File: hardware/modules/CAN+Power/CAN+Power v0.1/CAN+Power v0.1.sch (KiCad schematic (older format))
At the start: 10 parts

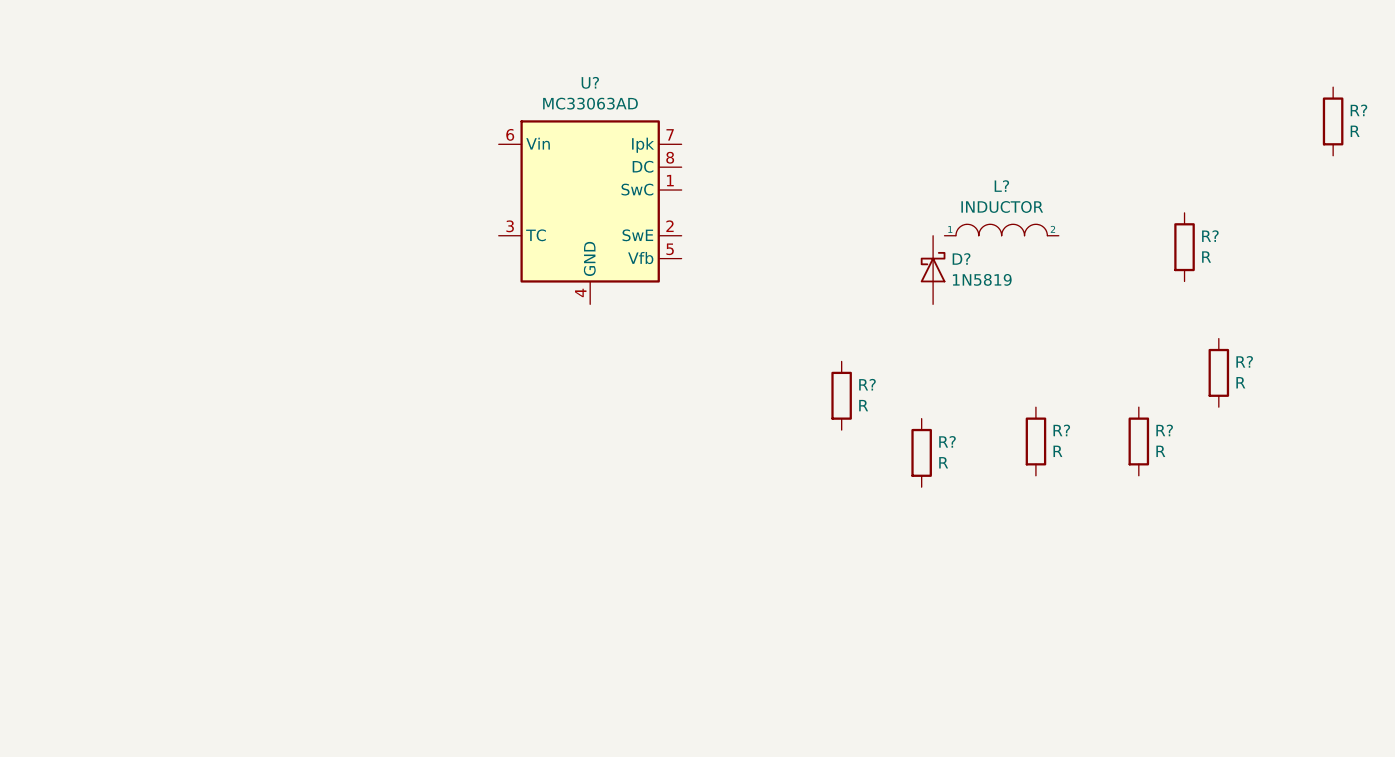
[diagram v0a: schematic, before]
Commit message: добавил керамику на входе, начал схему
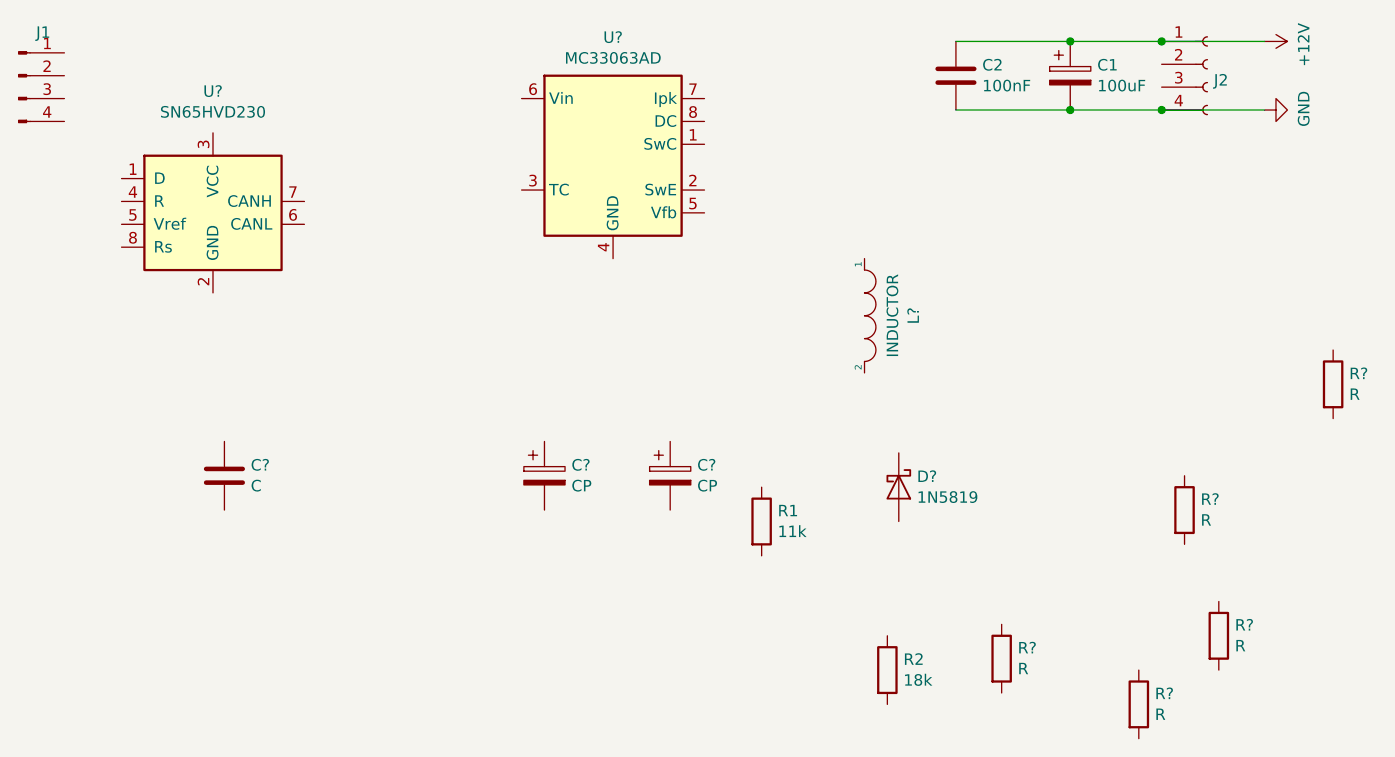
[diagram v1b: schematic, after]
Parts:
- added C1: 100uF, symbol Device:CP
- added C2: 100nF, symbol Device:C
- added C?: C, symbol Device:C
- added C? (x2): CP, symbol Device:CP
- added J1: Conn_01x04_Male, symbol Connector:Conn_01x04_Male
- added J2: 1, symbol Connector:Conn_01x04_Female
- added U?: SN65HVD230, Package_SO:SOIC-8_3.9x4.9mm_P1.27mm, symbol Interface_CAN_LIN:SN65HVD230
- R1: renamed from R?; value R -> 11k
- R2: renamed from R?; value R -> 18k
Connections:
- new net +12V: C1.1, C2.1, J2.1 (Pin_1)
- new net GND: C1.2, C2.2, J2.4 (Pin_4)
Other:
- moved on the sheet: D?, L?, R1, R2, R?, U?

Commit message: готова схема dc\dc
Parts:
- 220uF: renamed from C?; value CP -> C0
- Ct: renamed from C?; value C -> 270pF
- L1: renamed from L?; value INDUCTOR -> 47uH
- Rsc: renamed from R?; value R -> 0.3 Ohm
- gave numbers to parts that had none: 2
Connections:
- net +12V is gone; now on an unnamed net: C1.1, C2.1, J2.1 (Pin_1)
- net GND: now also 220uF.2, Ct.2, D?.2 (A), R1.2, U1.2 (GND), U2.4 (GND); no longer C1.2, C2.2, J2.4 (Pin_4)
- net at U2.1 (SwC): now also Rsc.2, U2.7 (Ipk), U2.8 (DC)
- net at U2.2 (SwE): now also D?.1 (K), L1.1
- net at U2.3 (TC): now also Ct.1
- net at U2.5 (Vfb): now also R1.1, R2.1
- net at U2.6 (Vin): now also Rsc.1
- net at L1.2: now also 220uF.1, R2.2
- new net: C1.2, C2.2, J2.4 (Pin_4)
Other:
- moved on the sheet: 220uF, C1, C2, C?, Ct, D?, J1, L1, R1, R2, R?, Rsc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

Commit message: готова
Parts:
- removed C?: CP, symbol Device:CP
- removed J1: Conn_01x04_Male, symbol Connector:Conn_01x04_Male
- removed R? (x3): R, symbol Device:R
- added C3: 100nF, symbol Device:C
- added C4, C5: 33pF, symbol Device:C
- added FL1: EMI_Filter_LL, symbol Device:EMI_Filter_LL
- added J1: Conn_01x05_Male, symbol Connector:Conn_01x05_Male
- Rterm: renamed from R?; value R -> 120 Ohm
- С0: renamed from 220uF; value C0 -> 220uF
- gave numbers to parts that had none: 1
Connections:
- net CANH: now also Rterm.2, C5.2, FL1.2
- net CANL: now also Rterm.1, C4.2, FL1.4
- net GND: now also C3.1, C4.1, C5.1, J1.1 (Pin_1)
- net 3.3+: now reaches L1.2, R2.2, С0.1
- net 3.3+: now also U1.3 (VCC), C3.2, J1.5 (Pin_5)
- net CAN_TXD: now reaches U1.1 (D)
- net CAN_TXD: now also J1.2 (Pin_2)
- net CAN_RXD: now reaches U1.4 (R)
- net CAN_RXD: now also J1.3 (Pin_3)
- net at U1.6 (CANL): now also FL1.3
- net at U1.7 (CANH): now also FL1.1
- net MODE: now reaches U1.8 (Rs)
- net MODE: now also J1.4 (Pin_4)
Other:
- moved on the sheet: C1, C2, Ct, D1, L1, R1, R2, Rsc, Rterm, U1, U2, С0

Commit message: готово
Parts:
- removed FL1: EMI_Filter_LL, symbol Device:EMI_Filter_LL
- C1: footprint (none) -> Capacitor_SMD:CP_Elec_6.3x5.4
- C2, C3, C4, C5: footprint (none) -> Capacitor_SMD:C_1206_3216Metric
- Ct1: renamed from Ct; footprint (none) -> Capacitor_SMD:C_1206_3216Metric
- J1: footprint (none) -> Connector_PinHeader_1.00mm:PinHeader_1x05_P1.00mm_Horizontal
- J2: footprint (none) -> Connector_Phoenix_MSTB:PhoenixContact_MSTBA_2,5_5-G_1x05_P5.00mm_Horizontal
- L1: footprint (none) -> Inductor_SMD:L_10.4x10.4_H4.8
- R1, R2: footprint (none) -> Resistor_SMD:R_1206_3216Metric
- Rsc1: renamed from Rsc; footprint (none) -> Resistor_SMD:R_1206_3216Metric
- Rterm1: renamed from Rterm; footprint (none) -> Resistor_SMD:R_1206_3216Metric
- С0: footprint (none) -> Capacitor_SMD:CP_Elec_8x10.5
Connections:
- net CANH: now also U1.7 (CANH)
- net CANL: now also U1.6 (CANL)
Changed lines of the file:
@@
 F 0 "R1" H 3070 3246 50  0000 L CNN
 F 1 "11k" H 3070 3155 50  0000 L CNN
-F 2 "" V 2930 3200 50  0001 C CNN
+F 2 "Resistor_SMD:R_1206_3216Metric" V 2930 3200 50  0001 C CNN
 F 3 "~" H 3000 3200 50  0001 C CNN
 	1    3000 3200
@@
 F 0 "R2" V 3720 3096 50  0000 L TNN
 F 1 "18k" V 3720 3005 50  0000 R TNN
-F 2 "" V 3580 3050 50  0001 C CNN
+F 2 "Resistor_SMD:R_1206_3216Metric" V 3580 3050 50  0001 C CNN
 F 3 "~" H 3650 3050 50  0001 C CNN
 	1    3650 3050
@@
 $EndComp
 $Comp
-L Device:R Rsc
+L Device:R Rsc1
 U 1 1 5E68F68F
 P 2600 1400
-F 0 "Rsc" V 2670 1446 50  0000 L TNN
+F 0 "Rsc1" V 2670 1446 50  0000 L TNN
 F 1 "0.3 Ohm" V 2670 1355 50  0000 R TNN
-F 2 "" V 2530 1400 50  0001 C CNN
+F 2 "Resistor_SMD:R_1206_3216Metric" V 2530 1400 50  0001 C CNN
 F 3 "~" H 2600 1400 50  0001 C CNN
 	1    2600 1400
@@
 $EndComp
 $Comp
-L Device:R Rterm
+L Device:R Rterm1
 U 1 1 5E68F74F
 P 4000 1550
-F 0 "Rterm" H 4070 1596 50  0000 L CNN
+F 0 "Rterm1" H 4070 1596 50  0000 L CNN
 F 1 "120 Ohm" H 4070 1505 50  0000 L CNN
-F 2 "" V 3930 1550 50  0001 C CNN
+F 2 "Resistor_SMD:R_1206_3216Metric" V 3930 1550 50  0001 C CNN
 F 3 "~" H 4000 1550 50  0001 C CNN
 	1    4000 1550
@@
 $EndComp
 $Comp
-L Device:C Ct
+L Device:C Ct1
 U 1 1 5E6907B8
 P 1850 2400
-F 0 "Ct" H 1965 2446 50  0000 L CNN
+F 0 "Ct1" H 1965 2446 50  0000 L CNN
 F 1 "270pF" H 1965 2355 50  0000 L CNN
-F 2 "" H 1888 2250 50  0001 C CNN
+F 2 "Capacitor_SMD:C_1206_3216Metric" H 1888 2250 50  0001 C CNN
 F 3 "~" H 1850 2400 50  0001 C CNN
 	1    1850 2400
@@
 F 0 "C1" H 1818 1296 50  0000 L CNN
 F 1 "100uF" H 1818 1205 50  0000 L CNN
-F 2 "" H 1738 1100 50  0001 C CNN
+F 2 "Capacitor_SMD:CP_Elec_6.3x5.4" H 1738 1100 50  0001 C CNN
 F 3 "~" H 1700 1250 50  0001 C CNN
 	1    1700 1250
@@
 F 0 "С0" H 4368 3246 50  0000 L CNN
 F 1 "220uF" H 4368 3155 50  0000 L CNN
-F 2 "" H 4288 3050 50  0001 C CNN
+F 2 "Capacitor_SMD:CP_Elec_8x10.5" H 4288 3050 50  0001 C CNN
 F 3 "~" H 4250 3200 50  0001 C CNN
 	1    4250 3200
@@
 F 0 "J2" H 1078 1230 50  0001 L CNN
 F 1 "1" H 1078 1185 50  0001 L CNN
-F 2 "" H 1050 1300 50  0001 C CNN
+F 2 "Connector_Phoenix_MSTB:PhoenixContact_MSTBA_2,5_5-G_1x05_P5.00mm_Horizontal" H 1050 1300 50  0001 C CNN
 F 3 "~" H 1050 1300 50  0001 C CNN
 	1    1050 1300
@@
 F 0 "C2" H 2315 1296 50  0000 L CNN
 F 1 "100nF" H 2315 1205 50  0000 L CNN
-F 2 "" H 2238 1100 50  0001 C CNN
+F 2 "Capacitor_SMD:C_1206_3216Metric" H 2238 1100 50  0001 C CNN
 F 3 "~" H 2200 1250 50  0001 C CNN
 	1    2200 1250
@@
 F 0 "L1" V 4171 2915 50  0000 C BNN
 F 1 "47uH" V 4250 2824 50  0000 L TNN
-F 2 "" H 4250 2700 50  0001 C CNN
+F 2 "Inductor_SMD:L_10.4x10.4_H4.8" H 4250 2700 50  0001 C CNN
 F 3 "~" H 4250 2700 50  0001 C CNN
 	1    4250 2700
@@
 F 0 "J1" H 6572 2878 50  0000 R BNN
 F 1 "Conn_01x05_Male" H 6708 3190 50  0001 C CNN
-F 2 "" H 6600 2900 50  0001 C CNN
+F 2 "Connector_PinHeader_1.00mm:PinHeader_1x05_P1.00mm_Horizontal" H 6600 2900 50  0001 C CNN
 F 3 "~" H 6600 2900 50  0001 C CNN
 	1    6600 2900
@@
 F 0 "C3" H 5665 2196 50  0000 L CNN
 F 1 "100nF" H 5665 2105 50  0000 L CNN
-F 2 "" H 5588 2000 50  0001 C CNN
+F 2 "Capacitor_SMD:C_1206_3216Metric" H 5588 2000 50  0001 C CNN
 F 3 "~" H 5550 2150 50  0001 C CNN
 	1    5550 2150
@@
 Wire Notes Line
 	5550 950  5550 1800
-Wire Wire Line
-	5400 1450 5400 1400
-Wire Wire Line
-	5400 1400 5600 1400
-Wire Wire Line
-	5400 1650 5400 1700
-Wire Wire Line
-	5400 1700 5600 1700
-Wire Wire Line
-	5000 1650 5000 1700
-Wire Wire Line
-	5000 1450 5000 1400
 $Comp
 L power:GND #PWR0108
@@
 F 0 "C5" H 4715 1246 39  0000 L CNN
 F 1 "33pF" H 4715 1155 39  0000 L CNN
-F 2 "" H 4638 1050 50  0001 C CNN
+F 2 "Capacitor_SMD:C_1206_3216Metric" H 4638 1050 50  0001 C CNN
 F 3 "~" H 4600 1200 50  0001 C CNN
 	1    4600 1200
@@
 F 0 "C4" H 5065 1246 39  0000 L CNN
 F 1 "33pF" H 5065 1155 39  0000 L CNN
-F 2 "" H 4988 1050 50  0001 C CNN
+F 2 "Capacitor_SMD:C_1206_3216Metric" H 4988 1050 50  0001 C CNN
 F 3 "~" H 4950 1200 50  0001 C CNN
 	1    4950 1200
@@
 Wire Notes Line
 	4450 950  5550 950
-$Comp
-L Device:EMI_Filter_LL FL1
-U 1 1 5E6DAE48
-P 5200 1550
-F 0 "FL1" H 5200 1772 50  0000 C TNN
-F 1 "EMI_Filter_LL" H 5200 1740 50  0001 C BNN
-F 2 "" H 5200 1590 50  0001 C CNN
-F 3 "~" H 5200 1590 50  0001 C CNN
-	1    5200 1550
-	-1   0    0    1
-$EndComp
 Wire Wire Line
 	4000 1400 4950 1400
@@
 Wire Wire Line
 	4600 1350 4600 1700
+Wire Wire Line
+	4950 1350 4950 1400
+Wire Wire Line
+	4950 1400 5600 1400
+Connection ~ 4950 1400
+Wire Wire Line
+	5600 1700 4600 1700
 Connection ~ 4600 1700
-Wire Wire Line
-	4600 1700 5000 1700
-Wire Wire Line
-	4950 1350 4950 1400
-Connection ~ 4950 1400
-Wire Wire Line
-	4950 1400 5000 1400
 $EndSCHEMATC
